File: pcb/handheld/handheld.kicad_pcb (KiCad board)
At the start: 2 copper layers, 100 x 69.9 mm, 65 parts, among them J1 Battery, J2 USB_C_Receptacle_USB2.0_16P, J3 Display Output, J4 Speaker ~(3W, 8R), J5 Joystick, J6 Debug, Q1 MMBT3904, SW1 SLW-1678105-6A-N-D, SW10 R, SW2 Reset, SW3 Boot, SW4 Select, SW5 A, SW6 B, SW7 X, SW8 Y, SW9 L, U1 ESP32-S3-WROOM-1, U2 AMS1117-3.3

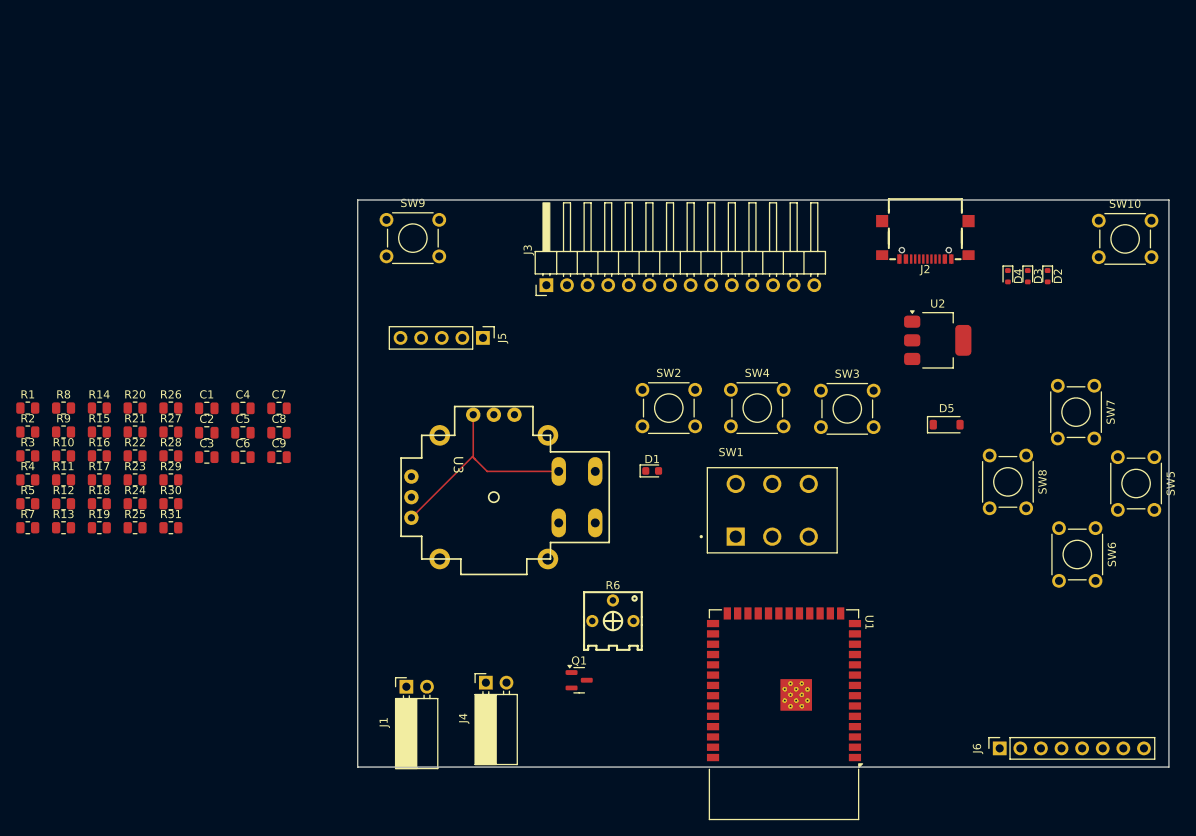
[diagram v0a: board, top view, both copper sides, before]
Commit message: Initial PCB routing
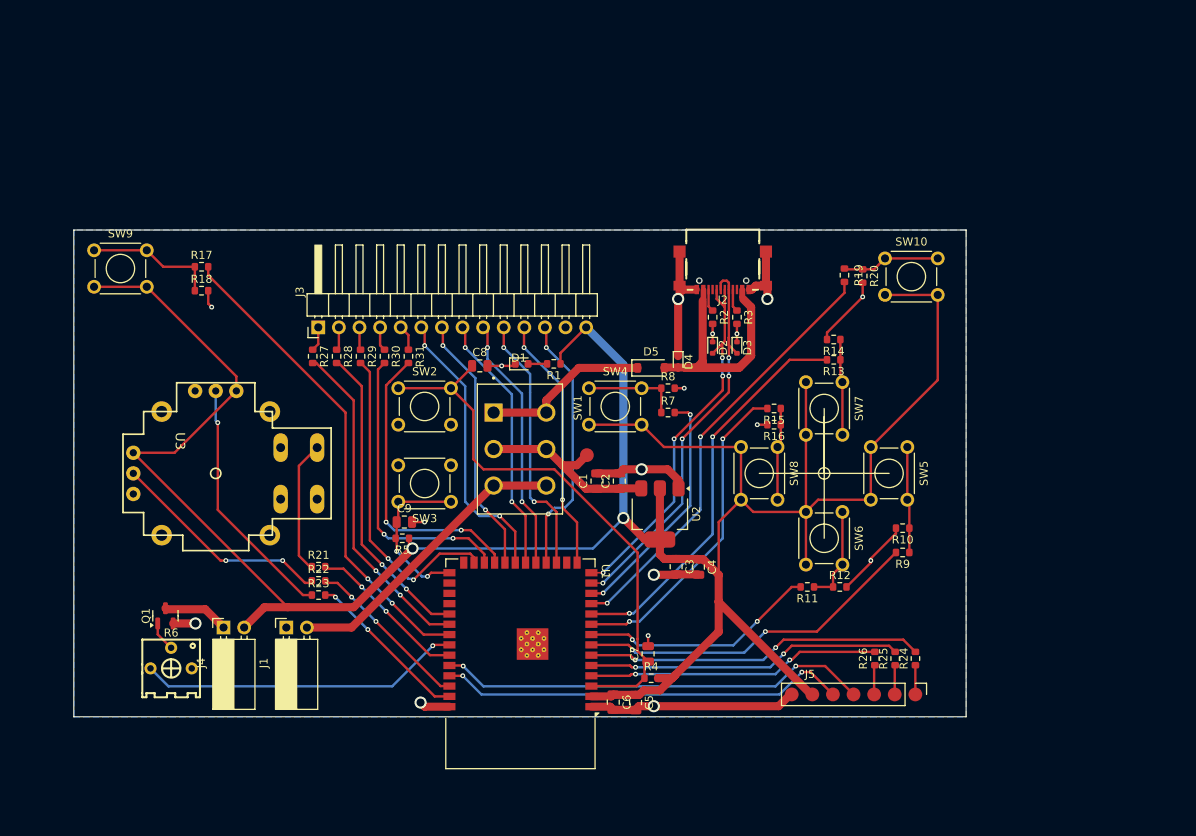
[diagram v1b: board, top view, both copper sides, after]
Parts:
- removed J6: Debug, Connector_PinSocket_2.54mm:PinSocket_1x08_P2.54mm_Vertical
- added TP1: V In, handheld:Testpoint, F.Cu at (158.2, 77.8)
- J5: value Joystick -> Debug; footprint Connector_PinHeader_2.54mm:PinHeader_1x05_P2.54mm_Vertical -> handheld:Header_1x07_P2.54mm_Pads
- R1, R10, R11, R12, R13, R14, R15, R16, R17, R18, R19, R2, R20, R21, R22, R23, R24, R25, R26, R27, R28, R29, R3, R30, R31, R4, R5, R7, R8, R9: footprint Resistor_SMD:R_0805_2012Metric -> Resistor_SMD:R_0603_1608Metric
- moved R9 104.5 mm to (197.2, 89.8), turned to 180 degrees
- moved R10 103.8 mm to (197.2, 86.8), turned to 180 degrees
- moved R24 98.1 mm to (198.8, 102.8), turned to 90 degrees
- moved R13 97.2 mm to (188.7, 66.0), turned to 180 degrees
- moved R19 97.0 mm to (190.0, 55.6), turned to -90 degrees
- moved R12 96.2 mm to (189.4, 94.0)
- moved R25 95.1 mm to (196.2, 102.8), turned to 90 degrees
- moved R11 92.6 mm to (185.4, 94.0), turned to 180 degrees
- moved R26 92.1 mm to (193.8, 102.8), turned to 90 degrees
- moved R20 91.2 mm to (192.2, 55.7), turned to -90 degrees
- moved R14 90.9 mm to (188.7, 63.5), turned to 180 degrees
- moved R3 89.1 mm to (176.8, 60.8), turned to -90 degrees
- moved R2 85.6 mm to (173.8, 60.8), turned to -90 degrees
- moved R16 83.3 mm to (181.3, 74.0), turned to 180 degrees
- moved R15 83.2 mm to (181.3, 72.0), turned to 180 degrees
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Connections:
- J3 pad 1: VCC -> Net-(J3-Pin_1)
- J3 pad 10: Net-(J3-Pin_10) -> DC/RS
- J3 pad 11: Net-(J3-Pin_11) -> Display Reset
- J3 pad 12: Net-(J3-Pin_12) -> CS
- J3 pad 13: Net-(J3-Pin_13) -> GND
- J3 pad 14: Net-(J3-Pin_14) -> VCC
- J3 pad 2: GND -> Net-(J3-Pin_2)
- J3 pad 3: CS -> Net-(J3-Pin_3)
- J3 pad 4: Display Reset -> Net-(J3-Pin_4)
- J3 pad 5: DC/RS -> Net-(J3-Pin_5)
- J3 pad 6: MOSI -> MISO
- J3 pad 7: SCK -> Backlight
- J3 pad 8: Backlight -> SCK
- J3 pad 9: MISO -> MOSI
- J4 pad 2: GND -> VCC
- J5 pad 1: VCC -> Net-(J5-Pin_1)
- J5 pad 4: Net-(J5-Pin_4) -> RX
- J5 pad 5: GND -> TX
- R24 pad 1: Net-(J6-Pin_8) -> Net-(J5-Pin_1)
- R24 pad 2: GPIO48 -> Spare 3
- R25 pad 1: Net-(J6-Pin_7) -> Net-(J5-Pin_2)
- R25 pad 2: GPIO38 -> Spare 2
- R26 pad 1: Net-(J6-Pin_6) -> Net-(J5-Pin_3)
- R26 pad 2: GPIO3 -> Spare 1
- R27 pad 1: Net-(J3-Pin_14) -> Net-(J3-Pin_1)
- R28 pad 1: Net-(J3-Pin_13) -> Net-(J3-Pin_2)
- R29 pad 1: Net-(J3-Pin_12) -> Net-(J3-Pin_3)
- R30 pad 1: Net-(J3-Pin_11) -> Net-(J3-Pin_4)
- R31 pad 1: Net-(J3-Pin_10) -> Net-(J3-Pin_5)
- U1 pad 10: Joystick X -> Button X
- U1 pad 11: Joystick Y -> Button R
- U1 pad 12: Joystick In -> Select
- U1 pad 15: GPIO3 -> Display Reset
- U1 pad 17: Display Reset -> DC/RS
- U1 pad 22: DC/RS -> Backlight
- U1 pad 23: Speaker -> T_CLK
- U1 pad 24: Select -> T_CS
- U1 pad 25: GPIO48 -> T_DIN
- U1 pad 31: GPIO38 -> T_DO
- U1 pad 32: Button A -> T_IRQ
- U1 pad 33: Button B -> Button L
- U1 pad 34: Button X -> Speaker
- U1 pad 35: Button Y -> Joystick In
- U1 pad 38: Button R -> Joystick Y
- U1 pad 39: Button L -> Joystick X
- U1 pad 4: T_CLK -> Spare 1
- U1 pad 5: T_CS -> Spare 2
- U1 pad 6: T_DIN -> Spare 3
- U1 pad 7: T_DO -> Button A
- U1 pad 8: T_IRQ -> Button B
- U1 pad 9: Backlight -> Button Y
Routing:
- net VCC: track 0.00 -> 330.2 mm, vias 0 -> 2
- net GND: track 27.7 -> 106.7 mm, vias 0 -> 17
- net RESET: track 0.00 -> 68.8 mm
- net Button L: track 0.00 -> 59.5 mm, vias 0 -> 2
- net Button R: track 0.00 -> 53.7 mm, vias 0 -> 2
- net RX: track 0.00 -> 53.4 mm, vias 0 -> 2
- net TX: track 0.00 -> 50.5 mm, vias 0 -> 2
- net D-: track 0.00 -> 49.3 mm, vias 0 -> 4
- net Button X: track 0.00 -> 49.1 mm, vias 0 -> 2
- net D+: track 0.00 -> 47.7 mm, vias 0 -> 4
- net Button A: track 0.00 -> 43.1 mm, vias 0 -> 2
- net Spare 3: track 0.00 -> 41.8 mm, vias 0 -> 2
- net Net-(D4-A2): track 0.00 -> 41.3 mm
- net T_IRQ: track 0.00 -> 40.9 mm, vias 0 -> 2
- net Button Y: track 0.00 -> 39.9 mm, vias 0 -> 2
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- added copper zone on B.Cu, net GND
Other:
- board size 100 x 69.9 mm -> 110 x 60 mm

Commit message: Updated components and shrunk width
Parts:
- added SW10: R, handheld:SW_B3F-3150_OMR, F.Cu at (143.8, 32.5)
- added SW9: L, handheld:SW_B3F-3150_OMR, F.Cu at (119.8, 30.0)
- J1, J4: footprint Connector_PinSocket_2.54mm:PinSocket_1x02_P2.54mm_Horizontal -> handheld:CONN_S2B-PH-K-S_JST
- J5: footprint handheld:Header_1x07_P2.54mm_Pads -> Connector_PinHeader_2.54mm:PinHeader_1x07_P2.54mm_Vertical
- R6: footprint handheld:RES-ADJ-TH_3P-L6.6-W7.0-P2.54-L_3362P -> handheld:PTV09A-4015F-B104_BRN
- SW2, SW3, SW4, SW5, SW6, SW7, SW8: footprint Button_Switch_THT:SW_TH_Tactile_Omron_B3F-100x -> handheld:SW_B3F-1050_OMR
- U3: value ~ -> Joystick Mount
- moved U3 2.50 mm to (115.0, 80.0)
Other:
- board size 110 x 60 mm -> 100 x 60 mm

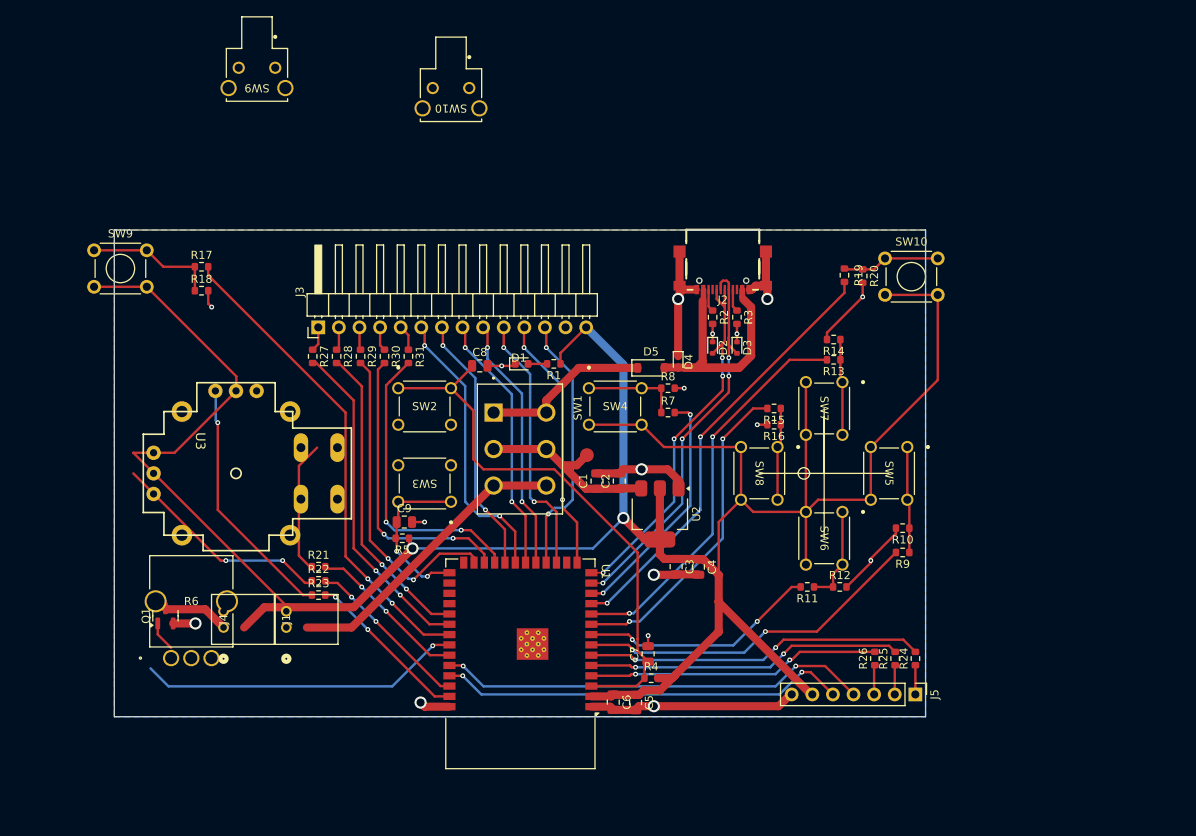
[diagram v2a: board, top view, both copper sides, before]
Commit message: Routed 4 layer design
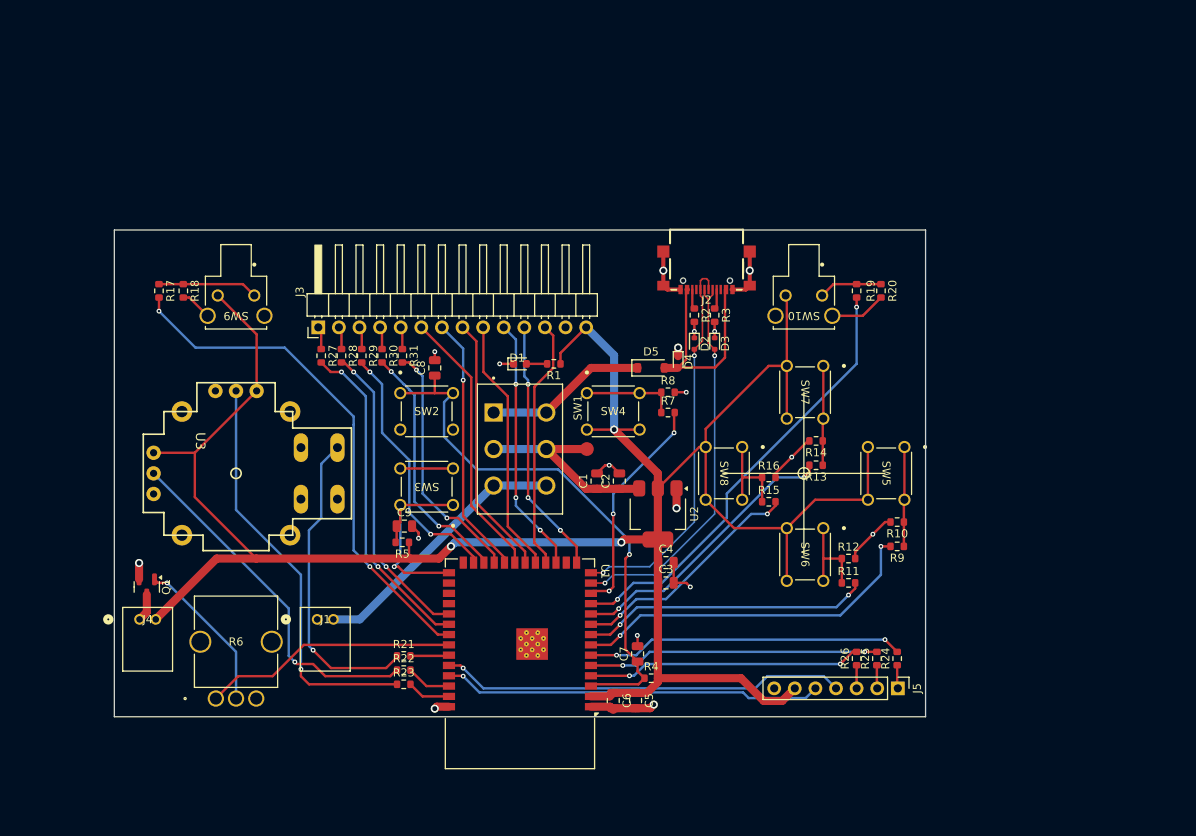
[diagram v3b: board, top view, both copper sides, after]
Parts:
- removed the SW10 at (195.0, 53.5)
- removed the SW9 at (97.5, 52.5)
- moved SW10 50.5 mm to (187.3, 58.1)
- moved SW9 28.2 mm to (117.3, 58.1)
- moved R21 15.2 mm to (135.7, 102.5)
- moved R22 15.2 mm to (135.7, 104.2)
- moved R23 15.2 mm to (135.7, 106.0)
- moved R13 13.2 mm to (186.5, 79.0)
- moved R14 12.7 mm to (186.5, 76.0)
- moved R15 11.5 mm to (180.7, 83.5), turned to 0 degrees
- moved J4 10.4 mm to (103.1, 98.0), turned to 0 degrees
- moved R6 7.43 mm to (112.5, 107.8)
- moved R16 6.53 mm to (180.7, 80.5), turned to 0 degrees
- moved R17 6.03 mm to (105.5, 57.5), turned to -90 degrees
- moved C8 5.56 mm to (139.5, 67.0), turned to 90 degrees
- moved R11 5.10 mm to (190.5, 93.5), turned to 0 degrees
- moved SW8 4.35 mm to (177.4, 76.8)
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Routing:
- net VCC: track 330.2 -> 282.7 mm, vias 2 -> 3
- net GND: track 106.7 -> 78.7 mm, vias 17 -> 18
- net Net-(U3-SEL+): track 16.5 -> 38.6 mm, vias 0 -> 1
- net Net-(U3-V): track 30.7 -> 50.7 mm
- net Net-(U3-H): track 27.6 -> 44.1 mm, vias 2 -> 1
- net Net-(Q1-B): track 3.68 -> 19.5 mm, vias 0 -> 1
- net Joystick X: track 20.5 -> 5.37 mm, vias 2 -> 0
- net Joystick Y: track 20.6 -> 5.57 mm, vias 2 -> 0
- net Joystick In: track 19.7 -> 4.79 mm, vias 2 -> 0
- net Net-(D4-A2): track 41.3 -> 26.6 mm
- net Button X: track 49.1 -> 35.0 mm
- net Button Y: track 39.9 -> 29.3 mm
- net Speaker: track 39.9 -> 31.5 mm, vias 1 -> 0
- net T_DIN: track 39.4 -> 31.8 mm
- net Button B: track 29.4 -> 35.7 mm
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- added copper zone on In1.Cu, net GND
- added copper zone on In2.Cu, net GND
- removed copper zone on B.Cu, net GND
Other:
- copper layers 2 -> 4

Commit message: Added drill holes and fixed some errors
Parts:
- moved R19 3.83 mm to (191.5, 61.3)
- moved R20 3.83 mm to (194.5, 61.3)
- moved R17 3.67 mm to (105.5, 61.2)
- moved R18 3.67 mm to (108.5, 61.2)
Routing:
- net Button R: track 55.0 -> 51.1 mm
- net Net-(R17-Pad1): track 12.3 -> 14.2 mm
- net Button L: track 63.6 -> 62.1 mm
- net GND: track 78.7 -> 77.8 mm
- net Select: vias 3 -> 2
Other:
- board size 100 x 60 mm -> 100 x 61 mm
